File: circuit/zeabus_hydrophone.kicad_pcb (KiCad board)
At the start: 4 copper layers, 100 x 70 mm, 161 parts, among them CN1 EPS.00.250.NTN, CN2 EPS.00.250.NTN, CN3 EPS.00.250.NTN, CN4 EPS.00.250.NTN, CON1 ZTEX-V2-FPGA, J1 JTAG, U1 AD9248, U10 MAX5387LAUD+T (10k), U11 MAX5387LAUD+T (10k), U2 AD9248, U3 REF1933, U4 OPA2365, U5 OPA2365, U6 ADA4940-2, U7 OPA2365, U8 OPA2365, U9 ADA4940-2

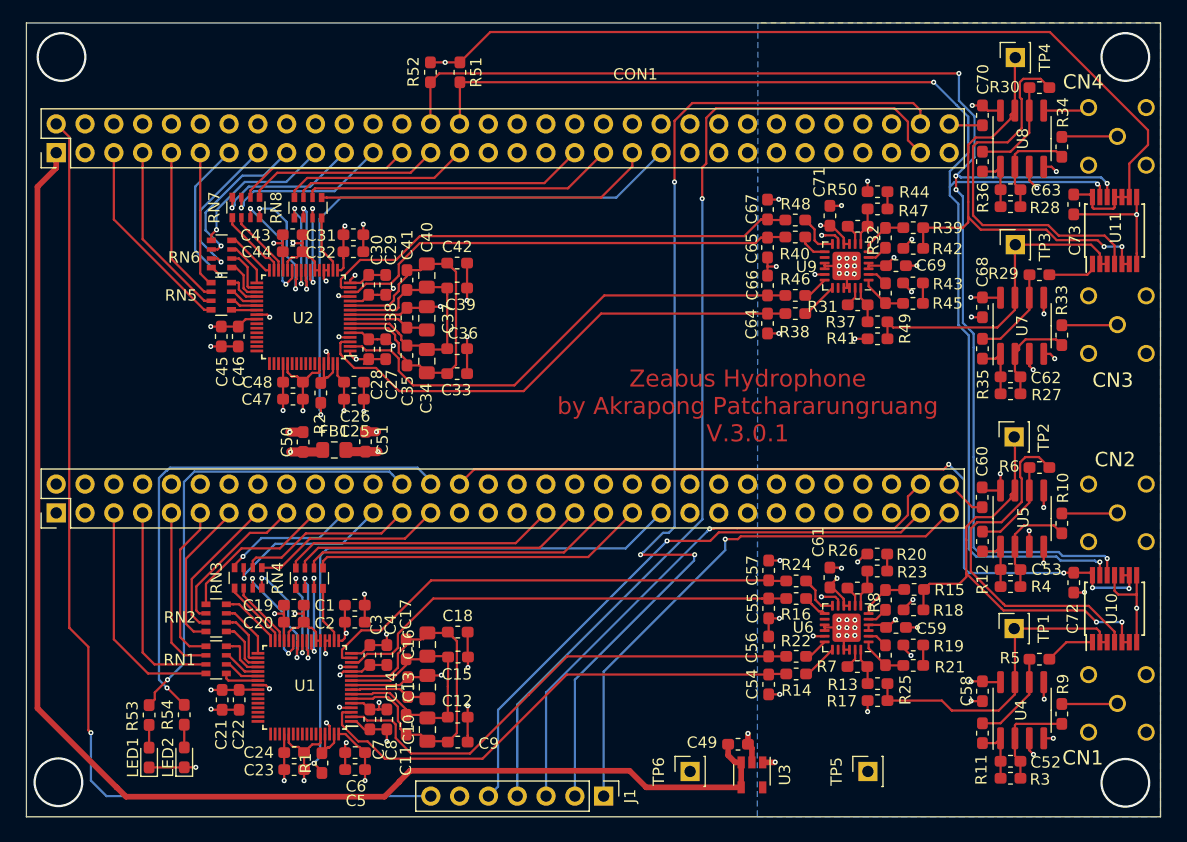
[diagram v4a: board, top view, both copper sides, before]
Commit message: Re-arrange and re-route PCB with some correction
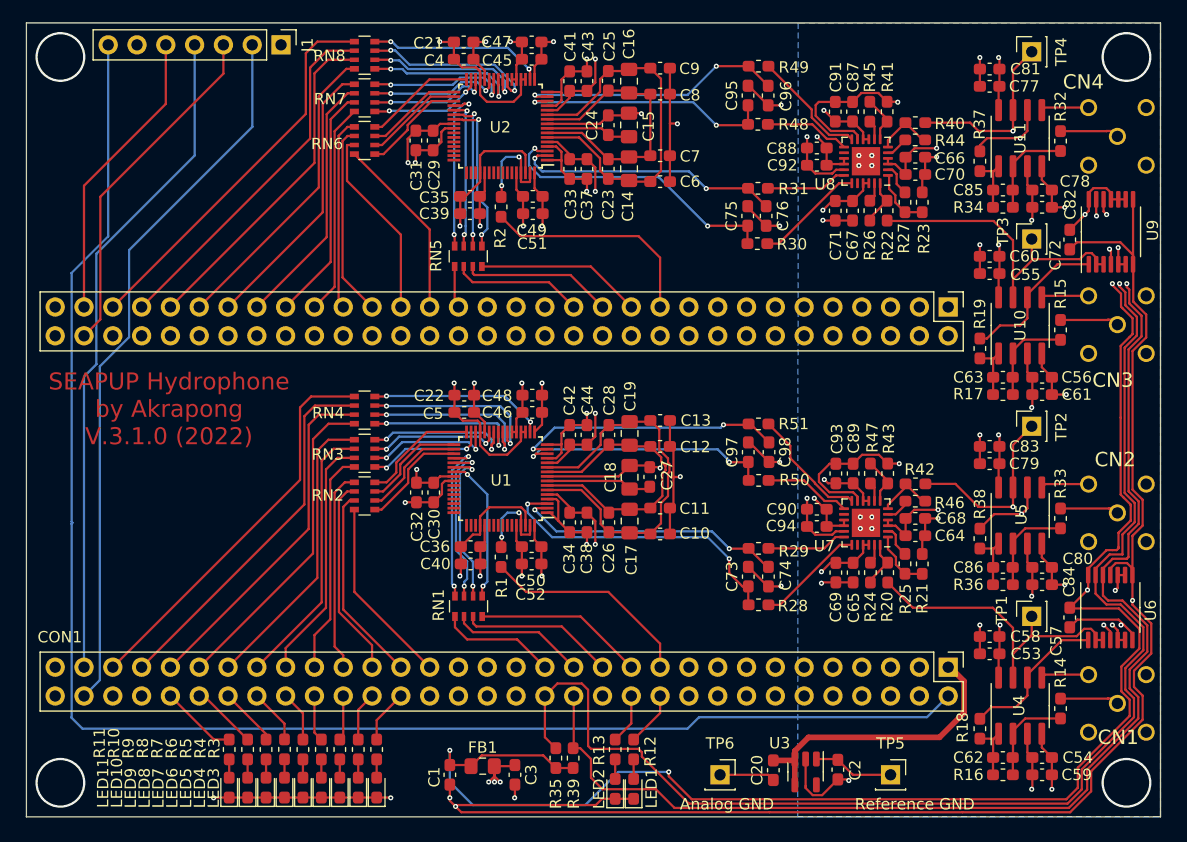
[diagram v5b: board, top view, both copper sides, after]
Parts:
- removed R52: 4.7k, Resistor_SMD:R_0603_1608Metric_Pad1.05x0.95mm_HandSolder
- removed R53, R54: 240, Resistor_SMD:R_0603_1608Metric_Pad1.05x0.95mm_HandSolder
- added C74: 2.7nF 1%(C0G), Capacitor_SMD:C_0603_1608Metric_Pad1.08x0.95mm_HandSolder, F.Cu at (143.4, 104.8)
- added C75: 2.7nF 1%(C0G), Capacitor_SMD:C_0603_1608Metric_Pad1.08x0.95mm_HandSolder, F.Cu at (141.6, 73.0)
- added C76: 2.7nF 1%(C0G), Capacitor_SMD:C_0603_1608Metric_Pad1.08x0.95mm_HandSolder, F.Cu at (143.2, 73.0)
- added C77: 0.01uF, Capacitor_SMD:C_0603_1608Metric_Pad1.08x0.95mm_HandSolder, F.Cu at (162.9, 61.6)
- added C78: 0.01uF, Capacitor_SMD:C_0603_1608Metric_Pad1.08x0.95mm_HandSolder, F.Cu at (167.6, 70.7)
- added C79: 0.01uF, Capacitor_SMD:C_0603_1608Metric_Pad1.08x0.95mm_HandSolder, F.Cu at (162.9, 94.9)
- added C80: 0.01uF, Capacitor_SMD:C_0603_1608Metric_Pad1.08x0.95mm_HandSolder, F.Cu at (167.6, 104.0)
- added C81: 0.1uF, Capacitor_SMD:C_0603_1608Metric_Pad1.08x0.95mm_HandSolder, F.Cu at (162.9, 60.1)
- added C82: 0.1uF, Capacitor_SMD:C_0603_1608Metric_Pad1.08x0.95mm_HandSolder, F.Cu at (167.6, 72.3)
- added C83: 0.1uF, Capacitor_SMD:C_0603_1608Metric_Pad1.08x0.95mm_HandSolder, F.Cu at (162.9, 93.3)
- added C84: 0.1uF, Capacitor_SMD:C_0603_1608Metric_Pad1.08x0.95mm_HandSolder, F.Cu at (167.6, 105.5)
- added C85: 100pF 1%(C0G), Capacitor_SMD:C_0603_1608Metric_Pad1.08x0.95mm_HandSolder, F.Cu at (164.1, 70.7)
- added C86: 100pF 1%(C0G), Capacitor_SMD:C_0603_1608Metric_Pad1.08x0.95mm_HandSolder, F.Cu at (164.1, 104.0)
- added C87: 0.01uF, Capacitor_SMD:C_0603_1608Metric_Pad1.08x0.95mm_HandSolder, F.Cu at (150.8, 63.8)
- added C88: 0.01uF, Capacitor_SMD:C_0603_1608Metric_Pad1.08x0.95mm_HandSolder, F.Cu at (147.7, 67.0)
- added C89: 0.01uF, Capacitor_SMD:C_0603_1608Metric_Pad1.08x0.95mm_HandSolder, F.Cu at (150.9, 95.7)
- added C90: 0.01uF, Capacitor_SMD:C_0603_1608Metric_Pad1.08x0.95mm_HandSolder, F.Cu at (147.7, 98.9)
- added C91: 0.1uF, Capacitor_SMD:C_0603_1608Metric_Pad1.08x0.95mm_HandSolder, F.Cu at (149.3, 63.8)
- added C92: 0.1uF, Capacitor_SMD:C_0603_1608Metric_Pad1.08x0.95mm_HandSolder, F.Cu at (147.7, 68.5)
- added C93: 0.1uF, Capacitor_SMD:C_0603_1608Metric_Pad1.08x0.95mm_HandSolder, F.Cu at (149.4, 95.7)
- added C94: 0.1uF, Capacitor_SMD:C_0603_1608Metric_Pad1.08x0.95mm_HandSolder, F.Cu at (147.7, 100.4)
- added C95: 2.7nF 1%(C0G), Capacitor_SMD:C_0603_1608Metric_Pad1.08x0.95mm_HandSolder, F.Cu at (141.6, 62.4)
- added C96: 2.7nF 1%(C0G), Capacitor_SMD:C_0603_1608Metric_Pad1.08x0.95mm_HandSolder, F.Cu at (143.4, 62.4)
- added C97: 2.7nF 1%(C0G), Capacitor_SMD:C_0603_1608Metric_Pad1.08x0.95mm_HandSolder, F.Cu at (141.7, 93.8)
- added C98: 2.7nF 1%(C0G), Capacitor_SMD:C_0603_1608Metric_Pad1.08x0.95mm_HandSolder, F.Cu at (143.5, 93.8)
- added LED10: YEL3, LED_SMD:LED_0603_1608Metric_Pad1.05x0.95mm_HandSolder, F.Cu at (97.5, 123.4)
- added LED11: GRE3, LED_SMD:LED_0603_1608Metric_Pad1.05x0.95mm_HandSolder, F.Cu at (95.9, 123.4)
- added LED3: RED1, LED_SMD:LED_0603_1608Metric_Pad1.05x0.95mm_HandSolder, F.Cu at (108.9, 123.4)
- added LED4: YEL1, LED_SMD:LED_0603_1608Metric_Pad1.05x0.95mm_HandSolder, F.Cu at (107.3, 123.4)
- added LED5: GRE1, LED_SMD:LED_0603_1608Metric_Pad1.05x0.95mm_HandSolder, F.Cu at (105.6, 123.4)
- added LED6: RED2, LED_SMD:LED_0603_1608Metric_Pad1.05x0.95mm_HandSolder, F.Cu at (104.0, 123.4)
- added LED7: YEL2, LED_SMD:LED_0603_1608Metric_Pad1.05x0.95mm_HandSolder, F.Cu at (102.4, 123.4)
- added LED8: GRE2, LED_SMD:LED_0603_1608Metric_Pad1.05x0.95mm_HandSolder, F.Cu at (100.8, 123.4)
- added LED9: RED3, LED_SMD:LED_0603_1608Metric_Pad1.05x0.95mm_HandSolder, F.Cu at (99.1, 123.4)
- C1, C21, C23, C25, C27, C3, C31, C43, C47, C7: value 0.01uF -> 0.1uF; footprint Capacitor_SMD:C_0603_1608Metric_Pad1.05x0.95mm_HandSolder -> Capacitor_SMD:C_0603_1608Metric_Pad1.08x0.95mm_HandSolder
- C10, C13, C37, C40: value 10uF -> 0.1uF; footprint Capacitor_SMD:C_0805_2012Metric_Pad1.15x1.40mm_HandSolder -> Capacitor_SMD:C_0603_1608Metric_Pad1.08x0.95mm_HandSolder
- C11, C12, C2, C20, C22, C24, C26, C28, C29, C32, C38, C39, C44, C45, C48, C5, C51, C58, C59, C6, C60, C61, C62, C63, C68, C69, C70, C71, C72, C8, C9: footprint Capacitor_SMD:C_0603_1608Metric_Pad1.05x0.95mm_HandSolder -> Capacitor_SMD:C_0603_1608Metric_Pad1.08x0.95mm_HandSolder
- C14, C15, C17, C18: value 0.1uF -> 10uF; footprint Capacitor_SMD:C_0603_1608Metric_Pad1.05x0.95mm_HandSolder -> Capacitor_SMD:C_0805_2012Metric_Pad1.18x1.45mm_HandSolder
- C16: footprint Capacitor_SMD:C_0805_2012Metric_Pad1.15x1.40mm_HandSolder -> Capacitor_SMD:C_0805_2012Metric_Pad1.18x1.45mm_HandSolder
- C19: value 0.01uF -> 10uF; footprint Capacitor_SMD:C_0603_1608Metric_Pad1.05x0.95mm_HandSolder -> Capacitor_SMD:C_0805_2012Metric_Pad1.18x1.45mm_HandSolder
- C30, C33, C35, C36, C4, C41, C42, C46, C49, C50: value 0.1uF -> 0.01uF; footprint Capacitor_SMD:C_0603_1608Metric_Pad1.05x0.95mm_HandSolder -> Capacitor_SMD:C_0603_1608Metric_Pad1.08x0.95mm_HandSolder
- C34: value 10uF -> 0.01uF; footprint Capacitor_SMD:C_0805_2012Metric_Pad1.15x1.40mm_HandSolder -> Capacitor_SMD:C_0603_1608Metric_Pad1.08x0.95mm_HandSolder
- C52: value 100pF 1%(C0G) -> 0.1uF; footprint Capacitor_SMD:C_0603_1608Metric_Pad1.05x0.95mm_HandSolder -> Capacitor_SMD:C_0603_1608Metric_Pad1.08x0.95mm_HandSolder
- C53: value 100pF 1%(C0G) -> 0.01uF; footprint Capacitor_SMD:C_0603_1608Metric_Pad1.05x0.95mm_HandSolder -> Capacitor_SMD:C_0603_1608Metric_Pad1.08x0.95mm_HandSolder
- C54, C55, C56, C64, C65, C66, C67: value 2.7nF 1%(C0G) -> 0.01uF; footprint Capacitor_SMD:C_0603_1608Metric_Pad1.05x0.95mm_HandSolder -> Capacitor_SMD:C_0603_1608Metric_Pad1.08x0.95mm_HandSolder
- C57: value 2.7nF 1%(C0G) -> 0.1uF; footprint Capacitor_SMD:C_0603_1608Metric_Pad1.05x0.95mm_HandSolder -> Capacitor_SMD:C_0603_1608Metric_Pad1.08x0.95mm_HandSolder
- C73: value 0.1uF -> 2.7nF 1%(C0G); footprint Capacitor_SMD:C_0603_1608Metric_Pad1.05x0.95mm_HandSolder -> Capacitor_SMD:C_0603_1608Metric_Pad1.08x0.95mm_HandSolder
- LED1: value BLUE -> GREEN
- LED2: value GREEN -> BLUE
- R10, R9: value 470 -> 240
- R11, R12, R13, R5, R6, R7, R8: value 1k -> 240
- R14: value 33 -> 470
- R15, R32: value 1k -> 470
- R16: value 33 -> 1.58M
- R17: value 30.1 -> 1.58M
- R18, R41, R42: value 30.1 -> 1k
- R19, R20, R43, R44: value 15 -> 1k
- R22, R24, R38, R40, R46: value 33 -> 1k
- R27: value 1.58M -> 1k
- R28: value 1.58M -> 33
- R29, R30, R31, R49, R50: value 1k -> 33
- R3, R4: value 1.58M -> 240
- R34: value 470 -> 1.58M
- R35, R39: value 1k -> 4.7k
- R36: value 1k -> 1.58M
- R51: value 4.7k -> 33
- U10, U11: value MAX5387LAUD+T (10k) -> OPA2365; footprint Package_SO:TSSOP-14_4.4x5mm_P0.65mm -> Package_SO:SOIC-8_3.9x4.9mm_P1.27mm
- U6, U9: value ADA4940-2 -> MAX5387LAUD+T (10k); footprint Package_CSP:LFCSP-24-1EP_4x4mm_P0.5mm_EP2.5x2.5mm -> Package_SO:TSSOP-14_4.4x5mm_P0.65mm
- U7, U8: value OPA2365 -> ADA4940-2; footprint Package_SO:SOIC-8_3.9x4.9mm_P1.27mm -> Package_CSP:LFCSP-24-1EP_4x4mm_P0.5mm_EP2.5x2.5mm
- moved R10 74.5 mm to (97.5, 120.1), turned to 90 degrees
- moved J1 72.1 mm to (100.5, 57.9)
- moved R9 70.2 mm to (99.1, 120.1), turned to 90 degrees
- moved R6 68.0 mm to (104.0, 120.1), turned to 90 degrees
- moved R11 66.4 mm to (95.9, 120.1), turned to 90 degrees
- moved R5 62.2 mm to (105.6, 120.1), turned to 90 degrees
- moved C9 62.0 mm to (133.9, 60.0)
- moved C24 61.9 mm to (129.3, 65.0), turned to 90 degrees
- moved C21 61.8 mm to (116.6, 57.7), turned to 0 degrees
- moved C8 60.2 mm to (133.9, 62.3), turned to 0 degrees
- moved C23 59.8 mm to (129.3, 68.9), turned to 90 degrees
- moved R4 59.3 mm to (107.3, 120.1), turned to 90 degrees
- moved C6 57.1 mm to (133.9, 70.0), turned to 0 degrees
- moved R3 55.9 mm to (108.9, 120.1), turned to 90 degrees
- moved C7 55.9 mm to (133.9, 67.7), turned to 0 degrees
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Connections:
- C1 pad 1: VDDA -> VDD
- C10 pad 2: /REFB1 -> GNDA
- C11 pad 1: /REFT1 -> /REFB1
- C11 pad 2: /REFB1 -> GNDA
- C13 pad 1: Net-(C13-Pad1) -> /REFT1
- C14 pad 1: Net-(C13-Pad1) -> /REFT2
- C14 pad 2: GNDA -> /REFB2
- C15 pad 1: /REFB1 -> Net-(C15-Pad1)
- C16 pad 1: /REFB1 -> /REFB2
- C16 pad 2: /REFT1 -> /REFT2
- C17 pad 1: /REFB1 -> /REFT1
- C17 pad 2: /REFT1 -> /REFB1
- C18 pad 1: /REFT1 -> Net-(C18-Pad1)
- C19 pad 1: VDD -> /REFB1
- C19 pad 2: GNDA -> /REFT1
- C2 pad 1: VDDA -> GNDA
- C2 pad 2: GNDA -> GNDREF
- C20 pad 1: VDD -> GNDA
- C20 pad 2: GNDA -> VBUS
- C23 pad 1: VDD -> /REFT2
- C23 pad 2: GNDA -> /REFB2
- C24 pad 1: VDD -> Net-(C15-Pad1)
- C25 pad 1: VDDA -> /REFB2
- C25 pad 2: GNDA -> /REFT2
- C26 pad 1: VDDA -> /REFT1
- C26 pad 2: GNDA -> /REFB1
- C27 pad 1: VDDA -> Net-(C18-Pad1)
- C28 pad 1: VDDA -> /REFB1
- C28 pad 2: GNDA -> /REFT1
- C29 pad 1: VDDA -> VDD
- C30 pad 1: VDDA -> VDD
- C31 pad 1: VDDA -> VDD
- C32 pad 1: VDDA -> VDD
- C33 pad 1: /REFT2 -> VDDA
- C34 pad 1: /REFT2 -> VDDA
- C34 pad 2: /REFB2 -> GNDA
- C35 pad 1: /REFT2 -> VDD
- C35 pad 2: /REFB2 -> GNDA
- C36 pad 1: /REFB2 -> VDD
- C37 pad 1: Net-(C37-Pad1) -> VDDA
- C38 pad 1: Net-(C37-Pad1) -> VDDA
- C39 pad 1: /REFB2 -> VDD
- C4 pad 1: VDDA -> VDD
- C40 pad 1: /REFB2 -> VDD
- C40 pad 2: /REFT2 -> GNDA
- C41 pad 1: /REFB2 -> VDDA
- C41 pad 2: /REFT2 -> GNDA
- C42 pad 1: /REFT2 -> VDDA
- C43 pad 1: VDD -> VDDA
- C44 pad 1: VDD -> VDDA
- C45 pad 1: VDD -> VDDA
- C46 pad 1: VDD -> VDDA
- C47 pad 1: VDD -> VDDA
- C48 pad 1: VDD -> VDDA
- C49 pad 1: GNDA -> VDDA
- C49 pad 2: VBUS -> GNDA
- C5 pad 1: VDDA -> VDD
- C50 pad 1: VDD -> VDDA
- C52 pad 1: Net-(C52-Pad1) -> VDDA
- C52 pad 2: Net-(C52-Pad2) -> GNDA
- C53 pad 1: Net-(C53-Pad1) -> VDDA
- C53 pad 2: Net-(C53-Pad2) -> GNDREF
- C54 pad 1: /analog/VIN1- -> GNDREF
- C55 pad 1: /analog/VIN2- -> VDDA
- C55 pad 2: GNDA -> GNDREF
- C56 pad 1: GNDA -> GNDREF
- C56 pad 2: /analog/VIN1+ -> GNDA
- C57 pad 2: /analog/VIN2+ -> VDD
- C58 pad 2: GNDA -> GNDREF
- C59 pad 1: VDDA -> GNDREF
- C6 pad 1: VDDA -> /REFT2
- C60 pad 2: GNDA -> GNDREF
- C61 pad 1: VDDA -> GNDREF
- C64 pad 1: /analog/VIN3- -> VDDA
- C64 pad 2: GNDA -> GNDREF
- C65 pad 1: /analog/VIN4- -> GNDREF
- C66 pad 1: GNDA -> VDDA
- C66 pad 2: /analog/VIN3+ -> GNDREF
- C67 pad 1: GNDA -> GNDREF
- C67 pad 2: /analog/VIN4+ -> GNDA
- C68 pad 2: GNDA -> GNDREF
- C69 pad 1: VDDA -> GNDREF
- C7 pad 1: VDDA -> /REFB2
- C70 pad 2: GNDA -> GNDREF
- C71 pad 1: VDDA -> GNDREF
- C73 pad 1: GNDA -> /analog/VIN1-
- C73 pad 2: VDD -> GNDA
- C8 pad 1: VDDA -> /REFB2
- C9 pad 1: /REFT1 -> /REFT2
- CON1 pad A1: Net-(CON1-PadA1) -> unconnected-(CON1-PadA1)
- CON1 pad A10: Net-(CON1-PadA10) -> unconnected-(CON1-PadA10)
- CON1 pad A17: Net-(CON1-PadA17) -> unconnected-(CON1-PadA17)
- CON1 pad A3: Net-(CON1-PadA3) -> unconnected-(CON1-PadA3)
- CON1 pad A4: Net-(CON1-PadA4) -> unconnected-(CON1-PadA4)
- CON1 pad A5: Net-(CON1-PadA5) -> unconnected-(CON1-PadA5)
- CON1 pad A6: Net-(CON1-PadA6) -> unconnected-(CON1-PadA6)
- CON1 pad A7: Net-(CON1-PadA7) -> unconnected-(CON1-PadA7)
- CON1 pad A8: Net-(CON1-PadA8) -> unconnected-(CON1-PadA8)
- CON1 pad A9: Net-(CON1-PadA9) -> unconnected-(CON1-PadA9)
- CON1 pad B1: Net-(CON1-PadB1) -> unconnected-(CON1-PadB1)
- CON1 pad B10: Net-(CON1-PadB10) -> unconnected-(CON1-PadB10)
- CON1 pad B11: Net-(CON1-PadB11) -> unconnected-(CON1-PadB11)
- CON1 pad B12: Net-(CON1-PadB12) -> unconnected-(CON1-PadB12)
- CON1 pad B13: Net-(CON1-PadB13) -> unconnected-(CON1-PadB13)
- CON1 pad B14: Net-(CON1-PadB14) -> unconnected-(CON1-PadB14)
- CON1 pad B17: Net-(CON1-PadB17) -> unconnected-(CON1-PadB17)
- CON1 pad B18: Net-(CON1-PadB18) -> unconnected-(CON1-PadB18)
- CON1 pad B19: Net-(CON1-PadB19) -> unconnected-(CON1-PadB19)
- CON1 pad B20: Net-(CON1-PadB20) -> unconnected-(CON1-PadB20)
- CON1 pad B21: Net-(CON1-PadB21) -> unconnected-(CON1-PadB21)
- CON1 pad B22: Net-(CON1-PadB22) -> unconnected-(CON1-PadB22)
- CON1 pad B23: Net-(CON1-PadB23) -> unconnected-(CON1-PadB23)
- CON1 pad B24: Net-(CON1-PadB24) -> unconnected-(CON1-PadB24)
- CON1 pad B25: Net-(CON1-PadB25) -> unconnected-(CON1-PadB25)
- CON1 pad B26: Net-(CON1-PadB26) -> unconnected-(CON1-PadB26)
- CON1 pad B27: Net-(CON1-PadB27) -> unconnected-(CON1-PadB27)
- CON1 pad B28: Net-(CON1-PadB28) -> unconnected-(CON1-PadB28)
- CON1 pad B29: Net-(CON1-PadB29) -> unconnected-(CON1-PadB29)
- CON1 pad B3: Net-(CON1-PadB3) -> unconnected-(CON1-PadB3)
- CON1 pad B30: Net-(CON1-PadB30) -> unconnected-(CON1-PadB30)
- CON1 pad B4: Net-(CON1-PadB4) -> unconnected-(CON1-PadB4)
- CON1 pad B5: Net-(CON1-PadB5) -> unconnected-(CON1-PadB5)
- CON1 pad B6: Net-(CON1-PadB6) -> unconnected-(CON1-PadB6)
- CON1 pad B7: Net-(CON1-PadB7) -> unconnected-(CON1-PadB7)
- CON1 pad B8: Net-(CON1-PadB8) -> unconnected-(CON1-PadB8)
- CON1 pad B9: Net-(CON1-PadB9) -> unconnected-(CON1-PadB9)
- CON1 pad C10: Net-(CON1-PadC10) -> unconnected-(CON1-PadC10)
- CON1 pad C16: Net-(CON1-PadC16) -> unconnected-(CON1-PadC16)
- CON1 pad C3: Net-(CON1-PadC3) -> unconnected-(CON1-PadC3)
- CON1 pad C4: Net-(CON1-PadC4) -> unconnected-(CON1-PadC4)
- CON1 pad C5: Net-(CON1-PadC5) -> unconnected-(CON1-PadC5)
- CON1 pad C6: Net-(CON1-PadC6) -> unconnected-(CON1-PadC6)
- CON1 pad C7: Net-(CON1-PadC7) -> unconnected-(CON1-PadC7)
- CON1 pad C8: Net-(CON1-PadC8) -> unconnected-(CON1-PadC8)
- CON1 pad C9: Net-(CON1-PadC9) -> unconnected-(CON1-PadC9)
- CON1 pad D10: Net-(CON1-PadD10) -> unconnected-(CON1-PadD10)
- CON1 pad D13: Net-(CON1-PadD13) -> unconnected-(CON1-PadD13)
- CON1 pad D16: Net-(CON1-PadD16) -> unconnected-(CON1-PadD16)
- CON1 pad D19: Net-(CON1-PadD19) -> unconnected-(CON1-PadD19)
- CON1 pad D29: Net-(CON1-PadD29) -> unconnected-(CON1-PadD29)
- CON1 pad D3: Net-(CON1-PadD3) -> unconnected-(CON1-PadD3)
- CON1 pad D30: Net-(CON1-PadD30) -> unconnected-(CON1-PadD30)
- CON1 pad D4: Net-(CON1-PadD4) -> unconnected-(CON1-PadD4)
- CON1 pad D5: Net-(CON1-PadD5) -> unconnected-(CON1-PadD5)
- CON1 pad D6: Net-(CON1-PadD6) -> unconnected-(CON1-PadD6)
- CON1 pad D7: Net-(CON1-PadD7) -> unconnected-(CON1-PadD7)
- CON1 pad D8: Net-(CON1-PadD8) -> unconnected-(CON1-PadD8)
- CON1 pad D9: Net-(CON1-PadD9) -> unconnected-(CON1-PadD9)
- R1 pad 1: Net-(CON1-PadA22) -> Net-(CON1-PadC11)
- R10 pad 1: Net-(CN2-Pad1) -> Net-(LED10-Pad2)
- R10 pad 2: Net-(C53-Pad1) -> Net-(CON1-PadD27)
- R11 pad 1: Net-(R11-Pad1) -> Net-(LED11-Pad2)
- R11 pad 2: Net-(C52-Pad2) -> Net-(CON1-PadD28)
- R12 pad 1: Net-(R12-Pad1) -> Net-(CON1-PadD11)
- R12 pad 2: Net-(C53-Pad2) -> Net-(LED1-Pad2)
- R13 pad 1: Net-(R13-Pad1) -> Net-(CON1-PadD12)
- R13 pad 2: /analog/VR1_L -> Net-(LED2-Pad2)
- R14 pad 1: /analog/VIN1- -> Net-(CN1-Pad1)
- R14 pad 2: Net-(R14-Pad2) -> Net-(C62-Pad1)
- R15 pad 1: Net-(R15-Pad1) -> Net-(CN3-Pad1)
- R15 pad 2: /analog/VR2_L -> Net-(C63-Pad1)
- R16 pad 1: /analog/VIN2- -> Net-(C62-Pad2)
- R16 pad 2: Net-(R16-Pad2) -> Net-(C62-Pad1)
- R17 pad 1: /analog/VR1_L -> Net-(C63-Pad2)
- R17 pad 2: GNDREF -> Net-(C63-Pad1)
- R18 pad 1: /analog/VR2_L -> /analog/VR1_H
- R18 pad 2: GNDREF -> Net-(C62-Pad2)
- R19 pad 1: GNDREF -> /analog/VR3_H
- R19 pad 2: Net-(R19-Pad2) -> Net-(C63-Pad2)
- R2 pad 1: Net-(CON1-PadC22) -> Net-(CON1-PadA11)
- R20 pad 1: GNDREF -> Net-(R20-Pad1)
- R20 pad 2: Net-(R20-Pad2) -> /analog/VR1_L
- R21 pad 2: Net-(R19-Pad2) -> GNDREF
- R22 pad 1: /analog/VIN1+ -> Net-(R22-Pad1)
- R22 pad 2: Net-(R22-Pad2) -> /analog/VR3_L
- R23 pad 2: Net-(R20-Pad2) -> GNDREF
- R24 pad 1: /analog/VIN2+ -> Net-(R24-Pad1)
- R24 pad 2: Net-(R24-Pad2) -> Net-(R20-Pad1)
- R26 pad 2: Net-(R23-Pad1) -> Net-(R22-Pad1)
- R27 pad 1: Net-(C62-Pad2) -> Net-(R27-Pad1)
- R27 pad 2: Net-(C62-Pad1) -> Net-(R23-Pad1)
- R28 pad 1: Net-(C63-Pad2) -> /analog/VIN1-
- R28 pad 2: Net-(C63-Pad1) -> Net-(R28-Pad2)
- R29 pad 1: /analog/VR3_H -> /analog/VIN1+
- R3 pad 1: Net-(C52-Pad2) -> Net-(LED3-Pad2)
- R3 pad 2: Net-(C52-Pad1) -> Net-(CON1-PadD20)
- R30 pad 1: /analog/VR4_H -> /analog/VIN3-
- R31 pad 1: Net-(R31-Pad1) -> /analog/VIN3+
- R32 pad 1: Net-(R32-Pad1) -> Net-(CN4-Pad1)
- R32 pad 2: Net-(R32-Pad2) -> Net-(C85-Pad1)
- R33 pad 1: Net-(CN3-Pad1) -> Net-(CN2-Pad1)
- R33 pad 2: Net-(C62-Pad1) -> Net-(C86-Pad1)
- R34 pad 1: Net-(CN4-Pad1) -> Net-(C85-Pad2)
- R34 pad 2: Net-(C63-Pad1) -> Net-(C85-Pad1)
- R35 pad 1: Net-(R29-Pad2) -> VDD
- R35 pad 2: Net-(C62-Pad2) -> /SCL
- R36 pad 1: Net-(R30-Pad2) -> Net-(C86-Pad2)
- R36 pad 2: Net-(C63-Pad2) -> Net-(C86-Pad1)
- R37 pad 1: Net-(R31-Pad2) -> /analog/VR4_H
- R37 pad 2: /analog/VR3_L -> Net-(C85-Pad2)
- R38 pad 1: /analog/VIN3- -> /analog/VR2_H
- R38 pad 2: Net-(R38-Pad2) -> Net-(C86-Pad2)
- R39 pad 1: Net-(R32-Pad2) -> VDD
- R39 pad 2: /analog/VR4_L -> /SDA
- R4 pad 1: Net-(C53-Pad2) -> Net-(LED4-Pad2)
- R4 pad 2: Net-(C53-Pad1) -> Net-(CON1-PadD21)
- R40 pad 1: /analog/VIN4- -> Net-(R40-Pad1)
- R40 pad 2: Net-(R40-Pad2) -> /analog/VR4_L
- R41 pad 1: /analog/VR3_L -> Net-(R41-Pad1)
- R42 pad 1: /analog/VR4_L -> Net-(R42-Pad1)
- R42 pad 2: GNDREF -> /analog/VR2_L
- R43 pad 1: GNDREF -> Net-(R43-Pad1)
- R43 pad 2: Net-(R43-Pad2) -> GNDREF
- R44 pad 1: GNDREF -> Net-(R44-Pad1)
- R44 pad 2: Net-(R44-Pad2) -> Net-(R40-Pad1)
- R45 pad 2: Net-(R43-Pad2) -> Net-(R41-Pad1)
- R46 pad 1: /analog/VIN3+ -> Net-(R46-Pad1)
- R46 pad 2: Net-(R46-Pad2) -> Net-(R42-Pad1)
- R47 pad 2: Net-(R44-Pad2) -> Net-(R43-Pad1)
- R48 pad 1: /analog/VIN4+ -> /analog/VIN4-
- R49 pad 1: Net-(R49-Pad1) -> /analog/VIN4+
- R49 pad 2: Net-(R45-Pad1) -> Net-(R49-Pad2)
- R5 pad 1: /analog/VR1_H -> Net-(LED5-Pad2)
- R5 pad 2: Net-(R11-Pad1) -> Net-(CON1-PadD22)
- R50 pad 1: Net-(R50-Pad1) -> /analog/VIN2-
- R50 pad 2: Net-(R47-Pad1) -> Net-(R50-Pad2)
- R51 pad 1: VDD -> /analog/VIN2+
- R51 pad 2: /SCL -> Net-(R51-Pad2)
- R6 pad 1: /analog/VR2_H -> Net-(LED6-Pad2)
- R6 pad 2: Net-(R12-Pad1) -> Net-(CON1-PadD23)
- R7 pad 1: Net-(R7-Pad1) -> Net-(LED7-Pad2)
- R7 pad 2: Net-(R13-Pad1) -> Net-(CON1-PadD24)
- R8 pad 1: Net-(R8-Pad1) -> Net-(LED8-Pad2)
- R8 pad 2: Net-(R15-Pad1) -> Net-(CON1-PadD25)
- R9 pad 1: Net-(CN1-Pad1) -> Net-(LED9-Pad2)
- R9 pad 2: Net-(C52-Pad1) -> Net-(CON1-PadD26)
- RN1 pad 5: Net-(CON1-PadA6) -> Net-(CON1-PadC15)
- RN1 pad 6: Net-(CON1-PadA5) -> Net-(CON1-PadC14)
- RN1 pad 7: Net-(CON1-PadA4) -> Net-(CON1-PadC13)
- RN1 pad 8: Net-(CON1-PadA3) -> Net-(CON1-PadC12)
- RN2 pad 5: Net-(CON1-PadA10) -> Net-(CON1-PadC22)
- RN2 pad 6: Net-(CON1-PadA9) -> Net-(CON1-PadC21)
- RN2 pad 7: Net-(CON1-PadA8) -> Net-(CON1-PadC20)
- RN2 pad 8: Net-(CON1-PadA7) -> Net-(CON1-PadC19)
- RN3 pad 5: Net-(CON1-PadA14) -> Net-(CON1-PadC26)
- RN3 pad 6: Net-(CON1-PadA13) -> Net-(CON1-PadC25)
- RN3 pad 7: Net-(CON1-PadA12) -> Net-(CON1-PadC24)
- RN3 pad 8: Net-(CON1-PadA11) -> Net-(CON1-PadC23)
- RN4 pad 5: Net-(CON1-PadA21) -> Net-(CON1-PadC30)
- RN4 pad 6: Net-(CON1-PadA20) -> Net-(CON1-PadC29)
- RN4 pad 7: Net-(CON1-PadA19) -> Net-(CON1-PadC28)
- RN4 pad 8: Net-(CON1-PadA18) -> Net-(CON1-PadC27)
- RN5 pad 5: Net-(CON1-PadC6) -> Net-(CON1-PadA18)
- RN5 pad 6: Net-(CON1-PadC5) -> Net-(CON1-PadA14)
- RN5 pad 7: Net-(CON1-PadC4) -> Net-(CON1-PadA13)
- RN5 pad 8: Net-(CON1-PadC3) -> Net-(CON1-PadA12)
- RN6 pad 5: Net-(CON1-PadC10) -> Net-(CON1-PadA22)
- RN6 pad 6: Net-(CON1-PadC9) -> Net-(CON1-PadA21)
- RN6 pad 7: Net-(CON1-PadC8) -> Net-(CON1-PadA20)
- RN6 pad 8: Net-(CON1-PadC7) -> Net-(CON1-PadA19)
- RN7 pad 5: Net-(CON1-PadC14) -> Net-(CON1-PadA26)
- RN7 pad 6: Net-(CON1-PadC13) -> Net-(CON1-PadA25)
- RN7 pad 7: Net-(CON1-PadC12) -> Net-(CON1-PadA24)
- RN7 pad 8: Net-(CON1-PadC11) -> Net-(CON1-PadA23)
- RN8 pad 5: Net-(CON1-PadC21) -> Net-(CON1-PadA30)
- RN8 pad 6: Net-(CON1-PadC20) -> Net-(CON1-PadA29)
- RN8 pad 7: Net-(CON1-PadC19) -> Net-(CON1-PadA28)
- RN8 pad 8: Net-(CON1-PadC15) -> Net-(CON1-PadA27)
- U1 pad 42: Net-(U1-Pad42) -> unconnected-(U1-Pad42)
- U1 pad 43: Net-(U1-Pad43) -> unconnected-(U1-Pad43)
- U1 pad 44: Net-(U1-Pad44) -> unconnected-(U1-Pad44)
- U1 pad 45: Net-(U1-Pad45) -> unconnected-(U1-Pad45)
- U1 pad 46: Net-(U1-Pad46) -> unconnected-(U1-Pad46)
- U1 pad 47: Net-(U1-Pad47) -> unconnected-(U1-Pad47)
- U1 pad 48: Net-(U1-Pad48) -> unconnected-(U1-Pad48)
- U1 pad 49: Net-(U1-Pad49) -> unconnected-(U1-Pad49)
- U1 pad 50: Net-(U1-Pad50) -> unconnected-(U1-Pad50)
- U1 pad 51: Net-(U1-Pad51) -> unconnected-(U1-Pad51)
- U1 pad 54: Net-(U1-Pad54) -> unconnected-(U1-Pad54)
- U1 pad 55: Net-(U1-Pad55) -> unconnected-(U1-Pad55)
- U1 pad 56: Net-(U1-Pad56) -> unconnected-(U1-Pad56)
- U1 pad 57: Net-(U1-Pad57) -> unconnected-(U1-Pad57)
- U1 pad 58: Net-(U1-Pad58) -> unconnected-(U1-Pad58)
- U1 pad 59: Net-(U1-Pad59) -> unconnected-(U1-Pad59)
- U1 pad 8: Net-(C13-Pad1) -> Net-(C18-Pad1)
- U10 pad 1: /analog/VR1_H -> Net-(C63-Pad2)
- U10 pad 2: /analog/VR1_L -> Net-(C63-Pad1)
- U10 pad 3: /analog/VR1_L -> GNDREF
- U10 pad 4: /analog/VR2_H -> GNDA
- U10 pad 5: /analog/VR2_L -> GNDREF
- U10 pad 6: /analog/VR2_L -> /analog/VR3_H
- U10 pad 7: GNDA -> /analog/VR3_L
- U10 pad 8: GNDA -> VDDA
- U11 pad 1: /analog/VR3_H -> Net-(C85-Pad2)
- U11 pad 2: /analog/VR3_L -> Net-(C85-Pad1)
- U11 pad 3: /analog/VR3_L -> GNDREF
- U11 pad 4: /analog/VR4_H -> GNDA
- U11 pad 5: /analog/VR4_L -> GNDREF
- U11 pad 6: /analog/VR4_L -> /analog/VR4_H
- U11 pad 7: GNDA -> /analog/VR4_L
- U11 pad 8: GNDA -> VDDA
- U2 pad 42: Net-(U2-Pad42) -> unconnected-(U2-Pad42)
- U2 pad 43: Net-(U2-Pad43) -> unconnected-(U2-Pad43)
- U2 pad 44: Net-(U2-Pad44) -> unconnected-(U2-Pad44)
- U2 pad 45: Net-(U2-Pad45) -> unconnected-(U2-Pad45)
- U2 pad 46: Net-(U2-Pad46) -> unconnected-(U2-Pad46)
- U2 pad 47: Net-(U2-Pad47) -> unconnected-(U2-Pad47)
- U2 pad 48: Net-(U2-Pad48) -> unconnected-(U2-Pad48)
- U2 pad 49: Net-(U2-Pad49) -> unconnected-(U2-Pad49)
- U2 pad 50: Net-(U2-Pad50) -> unconnected-(U2-Pad50)
- U2 pad 51: Net-(U2-Pad51) -> unconnected-(U2-Pad51)
- U2 pad 54: Net-(U2-Pad54) -> unconnected-(U2-Pad54)
- U2 pad 55: Net-(U2-Pad55) -> unconnected-(U2-Pad55)
- U2 pad 56: Net-(U2-Pad56) -> unconnected-(U2-Pad56)
- U2 pad 57: Net-(U2-Pad57) -> unconnected-(U2-Pad57)
- U2 pad 58: Net-(U2-Pad58) -> unconnected-(U2-Pad58)
- U2 pad 59: Net-(U2-Pad59) -> unconnected-(U2-Pad59)
- U2 pad 8: Net-(C37-Pad1) -> Net-(C15-Pad1)
- U3 pad 5: Net-(U3-Pad5) -> unconnected-(U3-Pad5)
- U4 pad 1: Net-(C52-Pad2) -> Net-(C62-Pad2)
- U4 pad 2: Net-(C52-Pad1) -> Net-(C62-Pad1)
- U4 pad 6: Net-(R11-Pad1) -> /analog/VR1_H
- U5 pad 1: Net-(C53-Pad2) -> Net-(C86-Pad2)
- U5 pad 2: Net-(C53-Pad1) -> Net-(C86-Pad1)
- U5 pad 6: Net-(R12-Pad1) -> /analog/VR2_H
- U6 pad 1: Net-(R21-Pad1) -> /analog/VR1_H
- U6 pad 10: VDDA -> VDD
- U6 pad 11: GNDREF -> GNDA
- U6 pad 12: Net-(R24-Pad2) -> /SDA
- U6 pad 13: Net-(R16-Pad2) -> /SCL
- U6 pad 14: Net-(U6-Pad14) -> VDD
- U6 pad 2: Net-(R25-Pad1) -> /analog/VR1_L
- U6 pad 3: VDDA -> /analog/VR1_L
- U6 pad 4: VDDA -> /analog/VR2_H
- U6 pad 5: Net-(R8-Pad1) -> /analog/VR2_L
- U6 pad 6: Net-(R15-Pad1) -> /analog/VR2_L
- U6 pad 7: Net-(R23-Pad1) -> GNDA
- U6 pad 8: Net-(R26-Pad1) -> GNDA
- U6 pad 9: VDDA -> VDD
- U7 pad 1: Net-(C62-Pad2) -> Net-(R21-Pad1)
- U7 pad 2: Net-(C62-Pad1) -> Net-(R25-Pad1)
- U7 pad 3: GNDREF -> VDDA
- U7 pad 4: GNDA -> VDDA
- U7 pad 5: GNDREF -> Net-(R46-Pad1)
- U7 pad 6: Net-(R29-Pad2) -> Net-(R42-Pad1)
- U7 pad 7: /analog/VR3_L -> Net-(R43-Pad1)
- U7 pad 8: VDDA -> Net-(R47-Pad1)
- U8 pad 1: Net-(C63-Pad2) -> Net-(R23-Pad1)
- U8 pad 2: Net-(C63-Pad1) -> Net-(R27-Pad1)
- U8 pad 3: GNDREF -> VDDA
- U8 pad 4: GNDA -> VDDA
- U8 pad 5: GNDREF -> Net-(R44-Pad1)
- U8 pad 6: Net-(R30-Pad2) -> Net-(R40-Pad1)
- U8 pad 7: /analog/VR4_L -> Net-(R41-Pad1)
- U8 pad 8: VDDA -> Net-(R45-Pad1)
- U9 pad 1: Net-(R45-Pad1) -> /analog/VR3_H
- U9 pad 10: VDDA -> VDD
- U9 pad 11: GNDREF -> VDD
- U9 pad 12: Net-(R48-Pad2) -> /SDA
- U9 pad 13: Net-(R40-Pad2) -> /SCL
- U9 pad 14: Net-(U9-Pad14) -> VDD
- U9 pad 2: Net-(R49-Pad1) -> /analog/VR3_L
- U9 pad 3: VDDA -> /analog/VR3_L
- U9 pad 4: VDDA -> /analog/VR4_H
- U9 pad 5: Net-(R32-Pad1) -> /analog/VR4_L
- U9 pad 6: Net-(R32-Pad2) -> /analog/VR4_L
- U9 pad 7: Net-(R47-Pad1) -> GNDA
- U9 pad 8: Net-(R50-Pad1) -> GNDA
- U9 pad 9: VDDA -> VDD
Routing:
- net GNDA: track 163.8 -> 361.1 mm, vias 67 -> 46
- net VBUS: track 121.1 -> 25.9 mm
- net GNDREF: track 31.2 -> 107.3 mm, vias 20 -> 16
- net /RESn: track 89.7 -> 139.6 mm, vias 1 -> 0
- net Net-(CON1-PadB14): track 46.0 -> 0.00 mm, vias 1 -> 0
- net Net-(CON1-PadB13): track 41.0 -> 0.00 mm, vias 1 -> 0
- net VDDA: track 62.9 -> 99.2 mm, vias 17 -> 19
- net Net-(CON1-PadC30): track 0.00 -> 34.9 mm
- net Net-(CON1-PadA22): track 51.3 -> 17.0 mm, vias 1 -> 0
- net Net-(CON1-PadA30): track 0.00 -> 34.1 mm
- net VDD: track 185.6 -> 219.5 mm, vias 16 -> 12
- net Net-(CON1-PadC22): track 50.9 -> 17.8 mm, vias 1 -> 0
- net Net-(CON1-PadC29): track 0.00 -> 32.9 mm
- net Net-(CON1-PadA29): track 0.00 -> 31.8 mm
- net Net-(CON1-PadC28): track 0.00 -> 30.8 mm
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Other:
- board text added: "Analog GND"
- board text added: "Reference GND"
- board text added: "SEAPUP Hydrophone by Akrapong V.3.1.0 (2022)"
- board text removed: "Zeabus Hydrophone by Akrapong Patchararungruang V.3.0.1"

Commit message: Change FPGA-board socket from THT to SMD
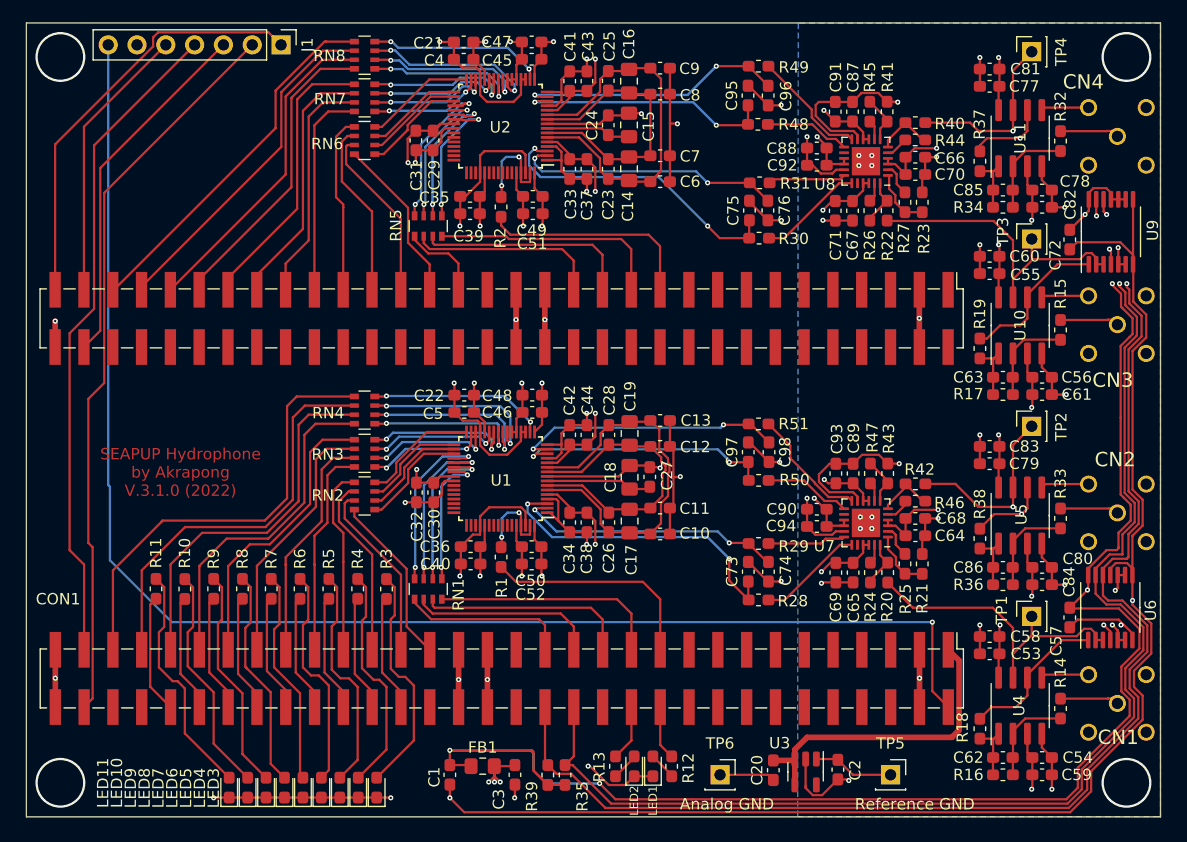
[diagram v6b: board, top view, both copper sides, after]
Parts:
- CON1: footprint zeabus:ZTEX-V2-FPGA -> zeabus:ZTEX-V2-FPGA-SMD
- moved R11 15.6 mm to (89.4, 105.9), turned to -90 degrees
- moved R10 15.2 mm to (92.0, 105.9), turned to -90 degrees
- moved R9 14.9 mm to (94.5, 105.9), turned to -90 degrees
- moved R8 14.6 mm to (97.0, 105.9), turned to -90 degrees
- moved R7 14.4 mm to (99.6, 105.9), turned to -90 degrees
- moved R6 14.3 mm to (102.1, 105.9), turned to -90 degrees
- moved R5 14.2 mm to (104.7, 105.9), turned to -90 degrees
- moved R3 14.2 mm to (109.8, 105.9), turned to -90 degrees
- moved R4 14.2 mm to (107.2, 105.9), turned to -90 degrees
- moved RN5 4.42 mm to (113.4, 73.9)
- moved RN1 3.87 mm to (113.4, 105.9)
- moved R12 3.67 mm to (134.9, 121.5)
- moved R39 2.68 mm to (124.0, 122.3)
- moved LED1 2.62 mm to (133.2, 121.5)
- moved LED2 2.60 mm to (131.6, 121.5)
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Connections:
- CON1 pad D14: /SDA -> /SCL
- CON1 pad D15: /SCL -> /SDA
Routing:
- net Net-(LED11-Pad2): track 1.61 -> 20.8 mm
- net Net-(LED3-Pad2): track 1.61 -> 20.5 mm
- net Net-(LED10-Pad2): track 1.61 -> 20.2 mm
- net Net-(LED4-Pad2): track 1.61 -> 20.2 mm
- net Net-(LED5-Pad2): track 1.61 -> 20.1 mm
- net GNDA: track 361.1 -> 379.4 mm, vias 46 -> 52
- net Net-(LED9-Pad2): track 1.61 -> 19.7 mm
- net Net-(LED6-Pad2): track 1.61 -> 19.6 mm
- net Net-(LED8-Pad2): track 1.63 -> 19.5 mm
- net Net-(LED7-Pad2): track 1.61 -> 19.1 mm
- net /RESn: track 139.6 -> 128.4 mm, vias 0 -> 1
- net VDD: track 219.5 -> 228.8 mm, vias 12 -> 14
- net /SCL: track 127.3 -> 119.4 mm
- net Net-(CON1-PadD22): track 3.97 -> 10.4 mm
- net Net-(CON1-PadD23): track 4.09 -> 10.4 mm
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
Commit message: Change mounting holes to m2-screws
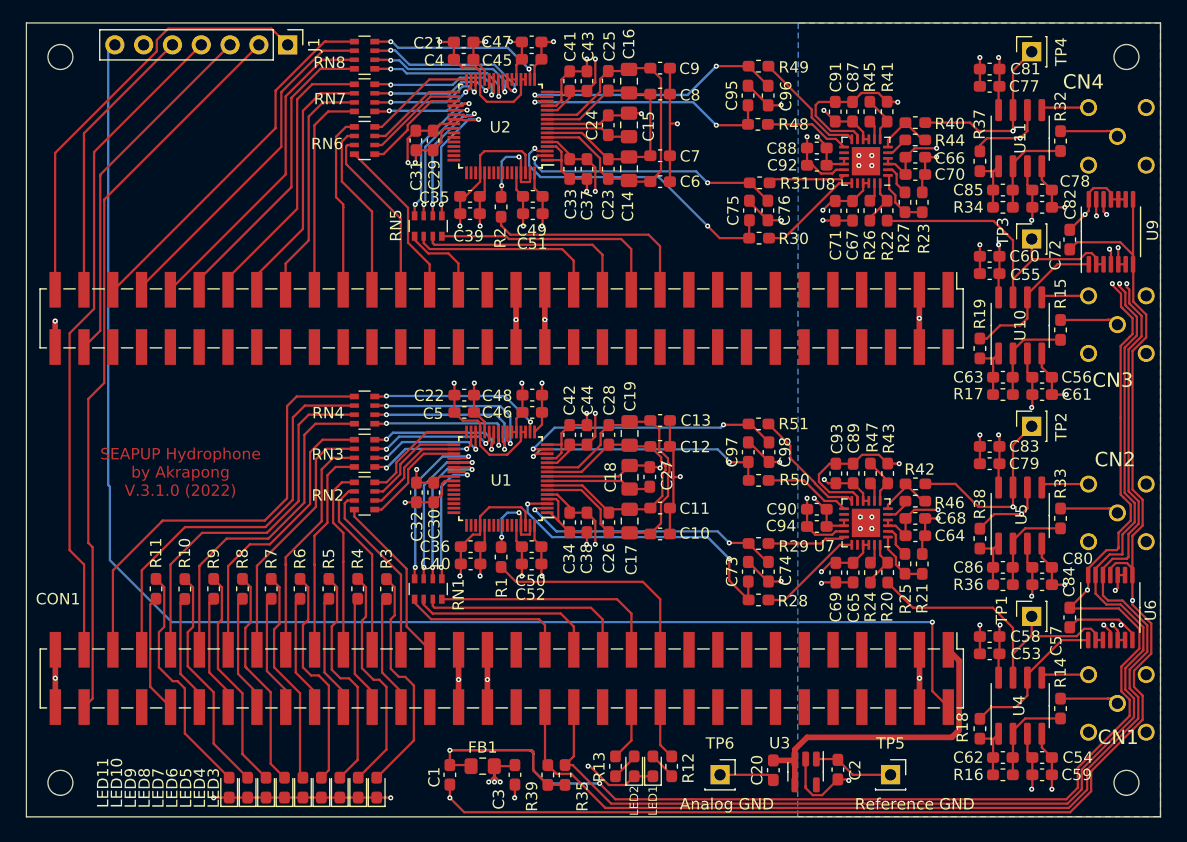
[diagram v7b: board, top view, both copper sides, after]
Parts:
- added REF**: MountingHole_2.2mm_M2, MountingHole:MountingHole_2.2mm_M2, F.Cu at (175.0, 59.0)
- added REF**: MountingHole_2.2mm_M2, MountingHole:MountingHole_2.2mm_M2, F.Cu at (81.0, 123.0)
- added REF**: MountingHole_2.2mm_M2, MountingHole:MountingHole_2.2mm_M2, F.Cu at (81.0, 59.0)
- added REF**: MountingHole_2.2mm_M2, MountingHole:MountingHole_2.2mm_M2, F.Cu at (175.0, 123.0)
- moved J1 0.59 mm to (101.0, 57.9)
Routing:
- net Net-(CON1-PadA32): track 37.7 -> 38.3 mm
- net (no net): vias 4 -> 0

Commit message: Finalized 2022 design with all gerber and bom
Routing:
- net VDDA: track 99.2 -> 97.4 mm
- net GNDA: track 379.4 -> 378.0 mm
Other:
- rule pad_to_mask_clearance: 0.051 -> 0
